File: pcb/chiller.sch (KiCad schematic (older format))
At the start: 10 parts

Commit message: Finish diagram; add Arduino code for display test.
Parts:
- removed RV?: POT, symbol POT
- removed U? (x2): DS18B20, symbol DS18B20
- removed U?: FLOW SENSOR, symbol DS18B20
- added BZ?: Buzzer, symbol Buzzer
- added C?: 100n, symbol C
- added D?: 1N4148, symbol DIODE
- added J? (x4): CONN_01X02, symbol CONN_01X02
- added J? (x3): CONN_01X03, symbol CONN_01X03
- added Q?: BC547, TO_SOT_Packages_THT:TO-92_Molded_Narrow, symbol BC547
- added R?: 1K, symbol R
- added R?: 100, symbol R
- added RL?: RM50-xx21, symbol RM50-xx21
- added RV?: 10K, symbol POT_TRIM
- C?: value CP -> 10u
- C?: value C -> 100n
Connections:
- net labels added: +12V
- net labels removed: +15V
- wire segments 58 -> 96
- no-connect marks 15 -> 16
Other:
- note added: "FAN"
- note added: "FLOW"
- note added: "LASERSAUR"
- note added: "PUMP"
- note added: "SSR"
- note added: "TEMP1"
- note added: "TEMP2"

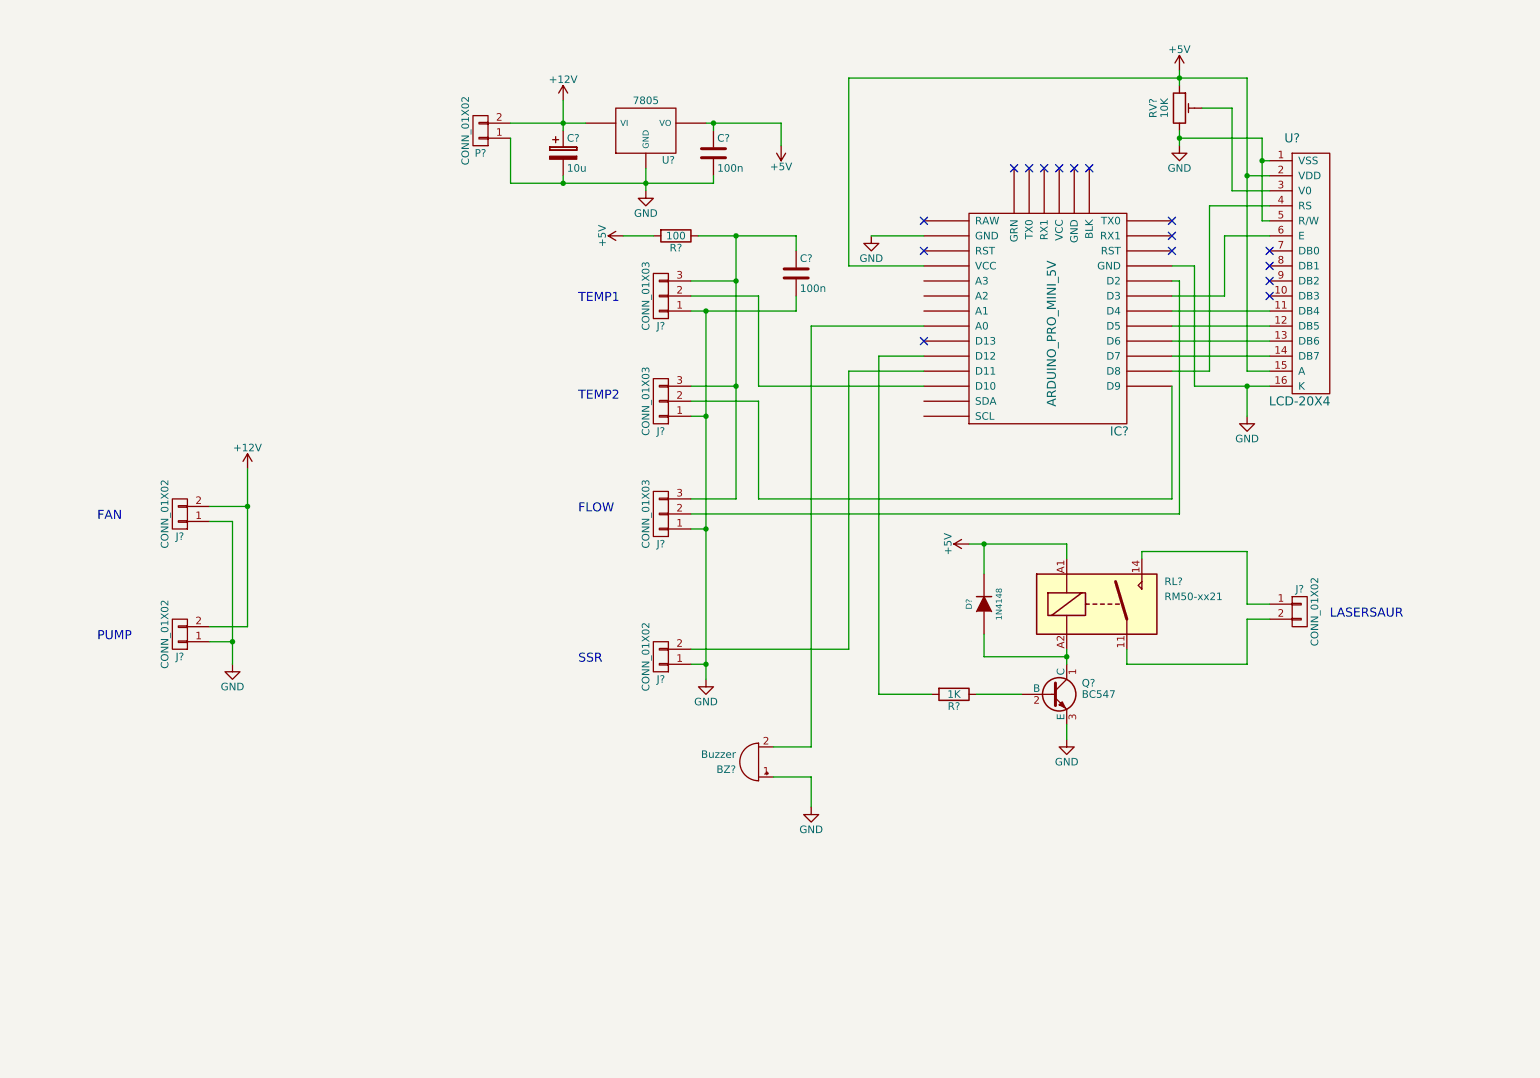
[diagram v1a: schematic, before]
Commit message: Add pullups, serial port connector.
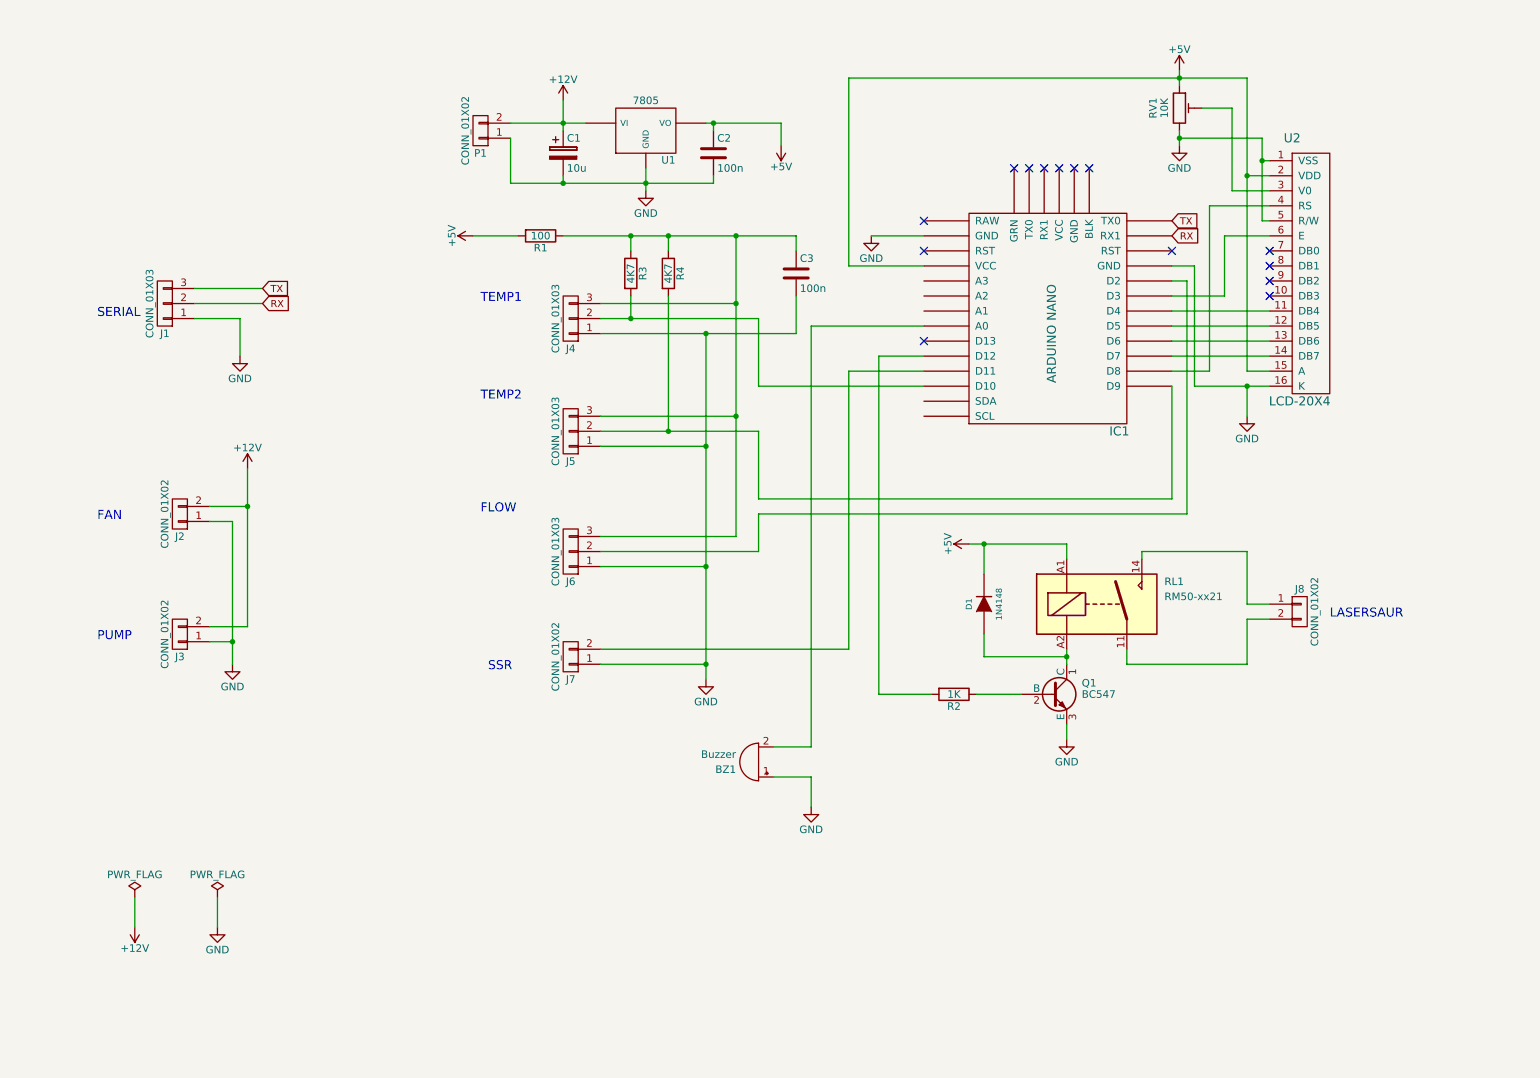
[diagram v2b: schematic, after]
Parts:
- added J1: CONN_01X03, symbol CONN_01X03
- added R3, R4: 4K7, symbol R
- IC1: renamed from IC?; value ARDUINO_PRO_MINI_5V -> ARDUINO NANO
- gave numbers to parts that had none: 20
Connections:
- net GND: now also J1.1 (P1)
- net TX: now reaches IC1.~ (VCC)
- net TX: now also J1.3 (P3)
- net at IC1.~ (VCC), J4.2 (P2): now also R3.2
- net at IC1.~ (VCC), J5.2 (P2): now also R4.2
- net at C3.1, J4.3 (P3), J5.3 (P3)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: now also R3.1, R4.1
- new net RX: IC1.~ (VCC), J1.2 (P2)
- no-connect marks 16 -> 14
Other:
- note added: "SERIAL"
- moved on the sheet: J4, J5, J6, J7, R1

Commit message: Add fan control. Drive SSR from 12V.
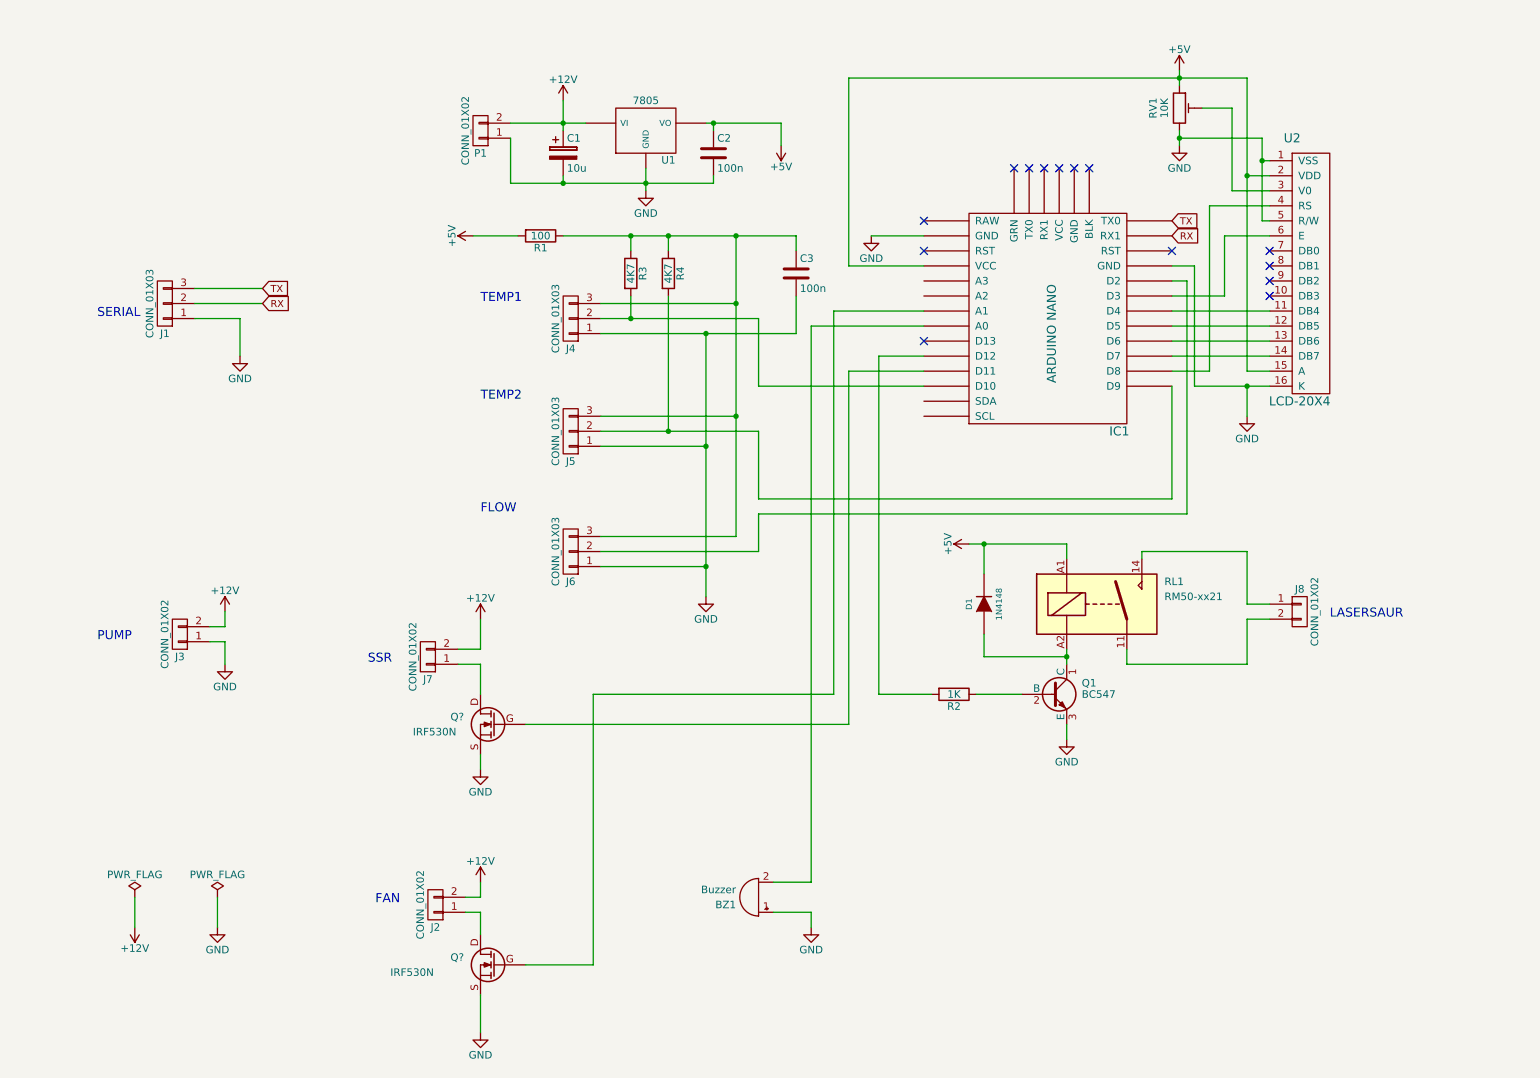
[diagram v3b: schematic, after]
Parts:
- added Q? (x2): IRF530N, symbol MOSFET_N_CH
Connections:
- net +12V: now also J7.2 (P2)
- net GND: now also Q?.S, Q?.S; no longer J2.1 (P1), J7.1 (P1)
- new net: IC1.~ (VCC), Q?.G (x2)
- new net: J7.1 (P1), Q?.D
- new net: J2.1 (P1), Q?.D
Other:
- moved on the sheet: BZ1, J2, J7
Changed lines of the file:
@@
 L GND #PWR9
 U 1 1 582F736C
-P 5200 4900
-F 0 "#PWR9" H 5200 4650 50  0001 C CNN
-F 1 "GND" H 5200 4750 50  0000 C CNN
-F 2 "" H 5200 4900 50  0000 C CNN
-F 3 "" H 5200 4900 50  0000 C CNN
-	1    5200 4900
+P 5200 4350
+F 0 "#PWR9" H 5200 4100 50  0001 C CNN
+F 1 "GND" H 5200 4200 50  0000 C CNN
+F 2 "" H 5200 4350 50  0000 C CNN
+F 3 "" H 5200 4350 50  0000 C CNN
+	1    5200 4350
 	1    0    0    -1
 $EndComp
@@
 	4500 2600 5800 2600
 Wire Wire Line
-	5200 2600 5200 4900
-Wire Wire Line
 	4500 3350 5200 3350
 Connection ~ 5200 3350
 Wire Wire Line
-	4500 4150 5200 4150
+	5200 4150 4500 4150
 Connection ~ 5200 4150
 Wire Wire Line
@@
 L CONN_01X02 J7
 U 1 1 58D195B3
-P 4300 4750
-F 0 "J7" H 4300 4900 50  0000 C CNN
-F 1 "CONN_01X02" V 4400 4750 50  0000 C CNN
-F 2 "" H 4300 4750 50  0001 C CNN
-F 3 "" H 4300 4750 50  0001 C CNN
-	1    4300 4750
+P 3350 4750
+F 0 "J7" H 3350 4900 50  0000 C CNN
+F 1 "CONN_01X02" V 3450 4750 50  0000 C CNN
+F 2 "" H 3350 4750 50  0001 C CNN
+F 3 "" H 3350 4750 50  0001 C CNN
+	1    3350 4750
 	-1   0    0    1
 $EndComp
@@
 Text Notes 3700 3800 0    60   ~ 0
 FLOW
-Text Notes 3750 4850 0    60   ~ 0
+Text Notes 2950 4800 0    60   ~ 0
 SSR
-Wire Wire Line
-	4500 4800 5200 4800
-Connection ~ 5200 4800
 $Comp
 L Buzzer BZ1
 U 1 1 58D2E5F1
-P 5550 5450
-F 0 "BZ1" H 5700 5500 50  0000 L CNN
-F 1 "Buzzer" H 5700 5400 50  0000 L CNN
-F 2 "" V 5525 5550 50  0001 C CNN
-F 3 "" V 5525 5550 50  0001 C CNN
-	1    5550 5450
+P 5550 6350
+F 0 "BZ1" H 5700 6400 50  0000 L CNN
+F 1 "Buzzer" H 5700 6300 50  0000 L CNN
+F 2 "" V 5525 6450 50  0001 C CNN
+F 3 "" V 5525 6450 50  0001 C CNN
+	1    5550 6350
 	-1   0    0    1
 $EndComp
@@
 $EndComp
 Wire Wire Line
-	4500 4700 6150 4700
-Wire Wire Line
-	6150 4700 6150 2850
+	4000 5200 6150 5200
+Wire Wire Line
+	6150 5200 6150 2850
 Wire Wire Line
 	6150 2850 6650 2850
@@
 L CONN_01X02 J2
 U 1 1 58D2FE93
-P 1700 3800
-F 0 "J2" H 1700 3950 50  0000 C CNN
-F 1 "CONN_01X02" V 1800 3800 50  0000 C CNN
-F 2 "" H 1700 3800 50  0001 C CNN
-F 3 "" H 1700 3800 50  0001 C CNN
-	1    1700 3800
-	-1   0    0    1
-$EndComp
-Text Notes 1150 3850 0    60   ~ 0
+P 3400 6400
+F 0 "J2" H 3400 6550 50  0000 C CNN
+F 1 "CONN_01X02" V 3500 6400 50  0000 C CNN
+F 2 "" H 3400 6400 50  0001 C CNN
+F 3 "" H 3400 6400 50  0001 C CNN
+	1    3400 6400
+	-1   0    0    1
+$EndComp
+Text Notes 3000 6400 0    60   ~ 0
 FAN
 $Comp
@@
 L +12V #PWR5
 U 1 1 58D30293
-P 2150 3500
-F 0 "#PWR5" H 2150 3350 50  0001 C CNN
-F 1 "+12V" H 2150 3640 50  0000 C CNN
-F 2 "" H 2150 3500 50  0001 C CNN
-F 3 "" H 2150 3500 50  0001 C CNN
-	1    2150 3500
-	1    0    0    -1
-$EndComp
-Wire Wire Line
-	2150 3500 2150 4550
-Wire Wire Line
-	2150 4550 1900 4550
-Wire Wire Line
-	1900 3750 2150 3750
-Connection ~ 2150 3750
+P 2000 4450
+F 0 "#PWR5" H 2000 4300 50  0001 C CNN
+F 1 "+12V" H 2000 4590 50  0000 C CNN
+F 2 "" H 2000 4450 50  0001 C CNN
+F 3 "" H 2000 4450 50  0001 C CNN
+	1    2000 4450
+	1    0    0    -1
+$EndComp
 $Comp
 L GND #PWR3
 U 1 1 58D303D0
-P 2050 4800
-F 0 "#PWR3" H 2050 4550 50  0001 C CNN
-F 1 "GND" H 2050 4650 50  0000 C CNN
-F 2 "" H 2050 4800 50  0001 C CNN
-F 3 "" H 2050 4800 50  0001 C CNN
-	1    2050 4800
-	1    0    0    -1
-$EndComp
-Wire Wire Line
-	2050 3850 2050 4800
-Wire Wire Line
-	2050 3850 1900 3850
-Wire Wire Line
-	1900 4650 2050 4650
-Connection ~ 2050 4650
+P 2000 4800
+F 0 "#PWR3" H 2000 4550 50  0001 C CNN
+F 1 "GND" H 2000 4650 50  0000 C CNN
+F 2 "" H 2000 4800 50  0001 C CNN
+F 3 "" H 2000 4800 50  0001 C CNN
+	1    2000 4800
+	1    0    0    -1
+$EndComp
+Wire Wire Line
+	2000 4650 2000 4800
+Wire Wire Line
+	1900 4650 2000 4650
 Wire Wire Line
 	6650 2550 5900 2550
 Wire Wire Line
-	5900 2550 5900 5350
-Wire Wire Line
-	5900 5350 5650 5350
+	5900 2550 5900 6250
+Wire Wire Line
+	5900 6250 5650 6250
 $Comp
 L GND #PWR11
 U 1 1 58D42121
-P 5900 5750
-F 0 "#PWR11" H 5900 5500 50  0001 C CNN
-F 1 "GND" H 5900 5600 50  0000 C CNN
-F 2 "" H 5900 5750 50  0001 C CNN
-F 3 "" H 5900 5750 50  0001 C CNN
-	1    5900 5750
-	1    0    0    -1
-$EndComp
-Wire Wire Line
-	5650 5550 5900 5550
-Wire Wire Line
-	5900 5550 5900 5750
+P 5900 6550
+F 0 "#PWR11" H 5900 6300 50  0001 C CNN
+F 1 "GND" H 5900 6400 50  0000 C CNN
+F 2 "" H 5900 6550 50  0001 C CNN
+F 3 "" H 5900 6550 50  0001 C CNN
+	1    5900 6550
+	1    0    0    -1
+$EndComp
+Wire Wire Line
+	5650 6450 5900 6450
+Wire Wire Line
+	5900 6450 5900 6550
 Text GLabel 8300 1850 2    47   Input ~ 0
 TX
@@
 	4950 1950 4950 2050
 Connection ~ 4950 1950
+$Comp
+L MOSFET_N_CH Q?
+U 1 1 59162D17
+P 3800 5200
+F 0 "Q?" H 4100 5250 50  0000 R CNN
+F 1 "IRF530N" H 4350 5150 50  0000 R CNN
+F 2 "" H 4000 5300 50  0000 C CNN
+F 3 "" H 3800 5200 50  0000 C CNN
+	1    3800 5200
+	-1   0    0    -1
+$EndComp
+$Comp
+L +12V #PWR?
+U 1 1 59162F37
+P 3700 4500
+F 0 "#PWR?" H 3700 4350 50  0001 C CNN
+F 1 "+12V" H 3700 4640 50  0000 C CNN
+F 2 "" H 3700 4500 50  0001 C CNN
+F 3 "" H 3700 4500 50  0001 C CNN
+	1    3700 4500
+	1    0    0    -1
+$EndComp
+Wire Wire Line
+	3700 4500 3700 4700
+Wire Wire Line
+	3700 4700 3550 4700
+Wire Wire Line
+	3550 4800 3700 4800
+Wire Wire Line
+	3700 4800 3700 5000
+$Comp
+L GND #PWR?
+U 1 1 591630EF
+P 3700 5500
+F 0 "#PWR?" H 3700 5250 50  0001 C CNN
+F 1 "GND" H 3700 5350 50  0000 C CNN
+F 2 "" H 3700 5500 50  0001 C CNN
+F 3 "" H 3700 5500 50  0001 C CNN
+	1    3700 5500
+	1    0    0    -1
+$EndComp
+Wire Wire Line
+	3700 5500 3700 5400
+Wire Wire Line
+	5200 2600 5200 4350
+Wire Wire Line
+	1900 4550 2000 4550
+Wire Wire Line
+	2000 4550 2000 4450
+$Comp
+L MOSFET_N_CH Q?
+U 1 1 591638EA
+P 3800 6800
+F 0 "Q?" H 4100 6850 50  0000 R CNN
+F 1 "IRF530N" H 4500 6750 50  0000 R CNN
+F 2 "" H 4000 6900 50  0000 C CNN
+F 3 "" H 3800 6800 50  0000 C CNN
+	1    3800 6800
+	-1   0    0    -1
+$EndComp
+$Comp
+L GND #PWR?
+U 1 1 59163A75
+P 3700 7250
+F 0 "#PWR?" H 3700 7000 50  0001 C CNN
+F 1 "GND" H 3700 7100 50  0000 C CNN
+F 2 "" H 3700 7250 50  0001 C CNN
+F 3 "" H 3700 7250 50  0001 C CNN
+	1    3700 7250
+	1    0    0    -1
+$EndComp
+Wire Wire Line
+	3600 6450 3700 6450
+Wire Wire Line
+	3700 6450 3700 6600
+Wire Wire Line
+	3700 7000 3700 7250
+$Comp
+L +12V #PWR?
+U 1 1 59163CEF
+P 3700 6250
+F 0 "#PWR?" H 3700 6100 50  0001 C CNN
+F 1 "+12V" H 3700 6390 50  0000 C CNN
+F 2 "" H 3700 6250 50  0001 C CNN
+F 3 "" H 3700 6250 50  0001 C CNN
+	1    3700 6250
+	1    0    0    -1
+$EndComp
+Wire Wire Line
+	3700 6250 3700 6350
+Wire Wire Line
+	3700 6350 3600 6350
+Wire Wire Line
+	6650 2450 6050 2450
+Wire Wire Line
+	6050 2450 6050 5000
+Wire Wire Line
+	6050 5000 4450 5000
+Wire Wire Line
+	4450 5000 4450 6800
+Wire Wire Line
+	4450 6800 4000 6800
 $EndSCHEMATC

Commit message: Prepare for proper PCB.
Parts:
- removed BZ1: Buzzer, symbol Buzzer
- removed D1: 1N4148, symbol DIODE
- removed Q1: BC547, TO_SOT_Packages_THT:TO-92_Molded_Narrow, symbol BC547
- removed Q? (x2): IRF530N, symbol MOSFET_N_CH
- added D1: BAT54, Package_TO_SOT_SMD:SOT-23, symbol Diode:BAT54C
- added J9: CONN_01X02, Connectors_JST:JST_PH_B2B-PH-K_02x2.00mm_Straight, symbol tinkerforge:CONN_01X02
- added Q1, Q4: MMBT3904, TO_SOT_Packages_SMD:SOT-23, symbol tinkerforge:MMBTA42
- added Q2: BSS138, Package_TO_SOT_SMD:SOT-23, symbol Transistor_FET:BSS138
- added Q3: ZXMN4A06G, Package_TO_SOT_SMD:SOT-223-3_TabPin2, symbol Transistor_FET:BSP129
- added R5: R, Resistors_SMD:R_0603, symbol chiller-rescue:R
- C1: symbol CP -> chiller-rescue:CP
- C2, C3: footprint (none) -> Capacitors_SMD:C_0603; symbol C -> chiller-rescue:C
- IC1: symbol ARDUINO_PRO_MINI_5V -> arduino:ARDUINO_PRO_MINI_5V
- J1, J4, J5, J6: footprint (none) -> Connectors_JST:JST_PH_B3B-PH-K_03x2.00mm_Straight; symbol CONN_01X03 -> chiller-rescue:CONN_01X03
- J2, J3, J7, J8, P1: footprint (none) -> Connectors_JST:JST_PH_B2B-PH-K_02x2.00mm_Straight; symbol CONN_01X02 -> tinkerforge:CONN_01X02
- R1, R2, R3, R4: footprint (none) -> Resistors_SMD:R_0603; symbol R -> chiller-rescue:R
- RL1: symbol RM50-xx21 -> chiller-rescue:RM50-xx21
- RV1: symbol POT_TRIM -> chiller-rescue:POT_TRIM
- U1: value 7805 -> 78M05; footprint (none) -> libs:DPAK-3; symbol 7805 -> chiller-rescue:7805
- U2: footprint (none) -> Pin_Headers:Pin_Header_Straight_1x16_Pitch2.54mm; symbol LCD-20X4 -> tinkerforge:LCD-20X4
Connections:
- wire segments 120 -> 147
- no-connect marks 14 -> 20
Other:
- note added: "BUZZER"
